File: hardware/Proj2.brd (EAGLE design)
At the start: 102.5 x 78.7 mm, 20 parts

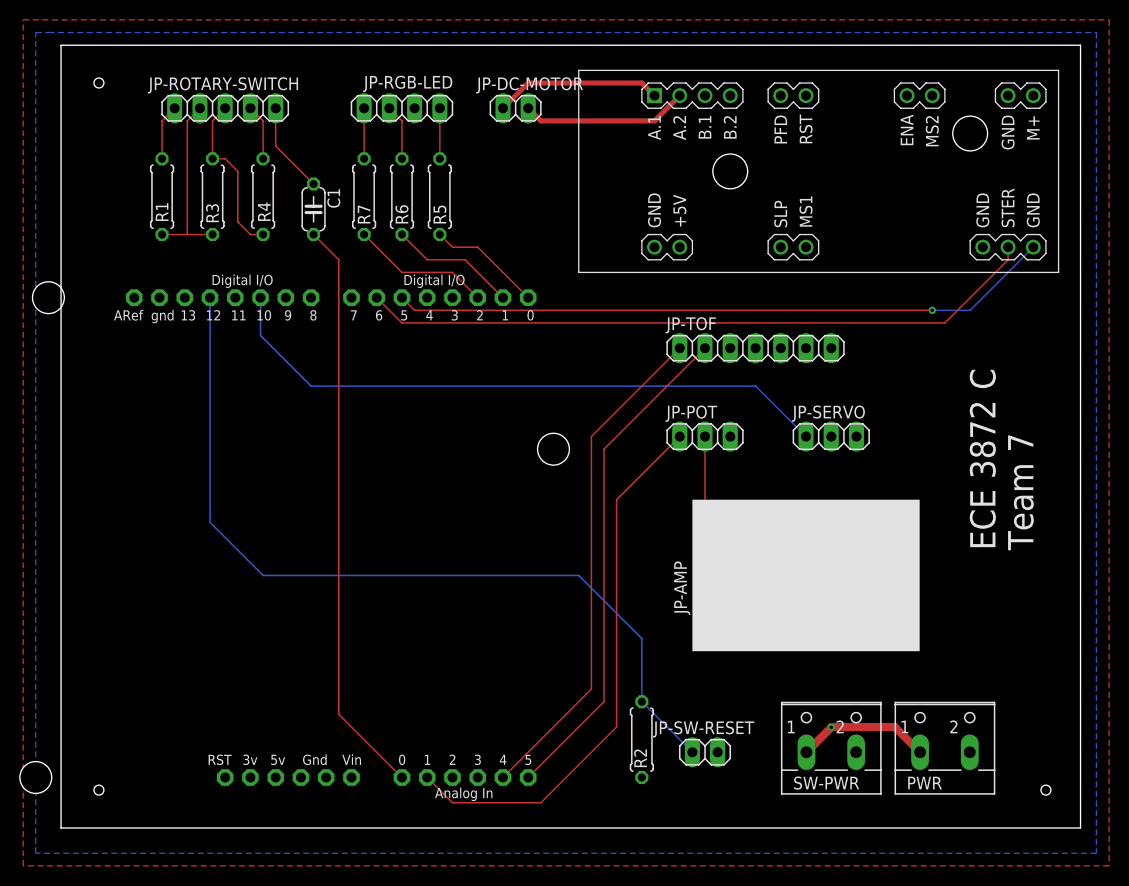
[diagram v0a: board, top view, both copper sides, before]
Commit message: Revisions from meeting, generate CAM files
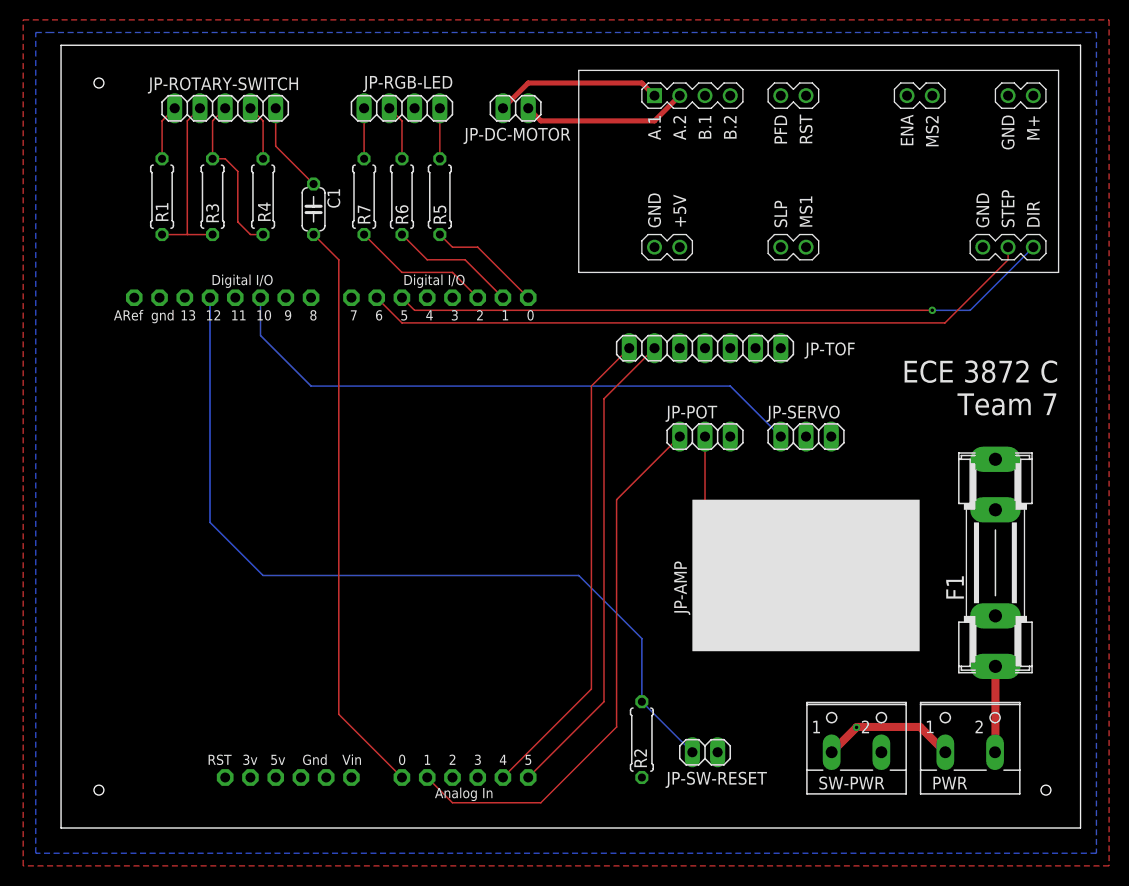
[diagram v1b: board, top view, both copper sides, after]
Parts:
- added F1: (no value), fuse:SHK20L
- U$1: value ARDUINO-BPLACE -> ARDUINO-NOHOLE; device adafruit:ARDUINO-BPLACE -> adafruit:ARDUINO-NOHOLE
- moved JP-TOF 5.08 mm to (64.8, 48.3)
- moved SW-PWR 2.54 mm to (80.0, 8.89)
- moved JP-SERVO 2.54 mm to (74.9, 39.4)
- moved PWR 2.54 mm to (91.4, 8.89)
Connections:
- new net N$5: F1.1A, PWR.2
- net GND: now also F1.2A; no longer PWR.2
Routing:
- net N$5: track 0.00 -> 8.65 mm
- net N$8: track 62.9 -> 60.3 mm
- net N$2: track 50.5 -> 48.4 mm
- net N$1: track 50.5 -> 48.4 mm

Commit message: Revise trace widths, power plane, fuse footprint after meeting with James
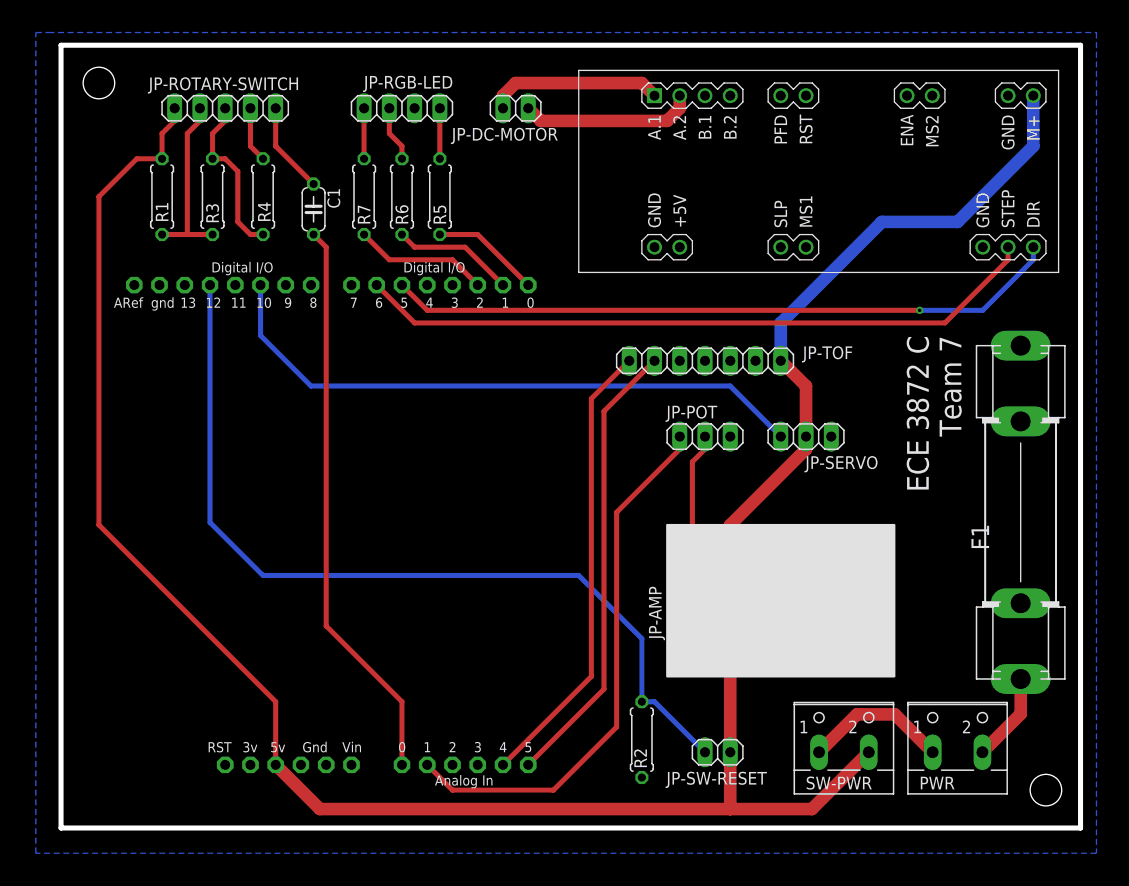
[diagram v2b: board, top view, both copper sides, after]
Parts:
- F1: device fuse:SHK20L -> fuse:SH32
- moved F1 5.68 mm to (96.5, 31.8)
- moved JP-AMP 3.59 mm to (63.5, 22.9)
- moved JP-SW-RESET 1.27 mm to (66.0, 7.62)
- moved SW-PWR 1.27 mm to (78.7, 8.89)
- moved U$1 1.27 mm to (-16.5, 3.81)
- moved JP-TOF 1.27 mm to (64.8, 47.0)
- moved PWR 1.27 mm to (90.2, 8.89)
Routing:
- net +5V: track 5.61 -> 236.7 mm
- net N$1: track 48.4 -> 45.9 mm
- net N$2: track 48.4 -> 45.9 mm
- net N$14: track 84.4 -> 87.0 mm
- net N$17: track 9.42 -> 12.0 mm
- net N$12: track 66.7 -> 67.9 mm
- net N$8: track 60.3 -> 61.6 mm
- net N$16: track 58.3 -> 57.0 mm
- net N$3: track 13.6 -> 14.6 mm, vias 1 -> 0
- net N$25: track 16.8 -> 17.6 mm
- net N$24: track 16.8 -> 17.6 mm
- net N$21: track 68.5 -> 69.0 mm
- net N$13: track 55.1 -> 54.6 mm
- net N$7: track 11.5 -> 11.0 mm
- net N$11: track 14.1 -> 13.5 mm
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- removed copper zone on layer 1, net +5V
